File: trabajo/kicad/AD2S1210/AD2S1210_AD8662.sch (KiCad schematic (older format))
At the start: 74 parts, among them IC1 AD8662, K1 JP_1, K2 V_control, K3 Power, P1 conn_stm32f4, P2 AOUT, P3 conn_motor_control, P4 JP_2, P5 JP_3, Q1 RECOM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

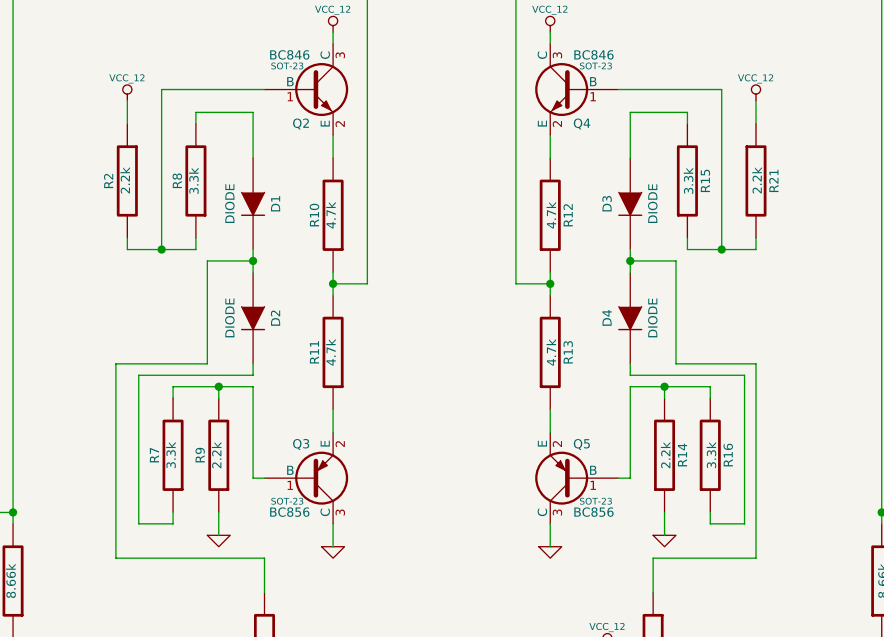
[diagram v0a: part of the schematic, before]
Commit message: correción de los valores de resistencias del buffer de tarjeta resolver
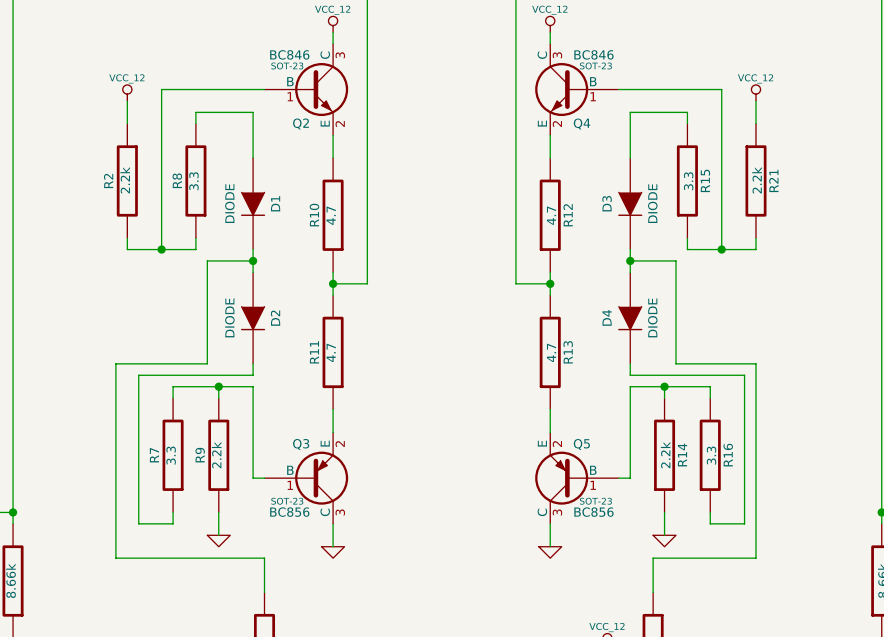
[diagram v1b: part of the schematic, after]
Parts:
- R10, R11, R12, R13: value 4.7k -> 4.7
- R15, R16, R7, R8: value 3.3k -> 3.3
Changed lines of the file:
@@
 Sheet 1 1
 Title "AD2S1210"
-Date "14 sep 2014"
+Date "13 mar 2015"
 Rev "V1.2"
 Comp "P. Koenig"
@@
 P 9900 1750
 F 0 "R15" V 9980 1750 40  0000 C CNN
-F 1 "3.3k" V 9907 1751 40  0000 C CNN
+F 1 "3.3" V 9907 1751 40  0000 C CNN
 F 2 "~" V 9830 1750 30  0000 C CNN
 F 3 "~" H 9900 1750 30  0000 C CNN
@@
 P 10000 2950
 F 0 "R16" V 10080 2950 40  0000 C CNN
-F 1 "3.3k" V 10007 2951 40  0000 C CNN
+F 1 "3.3" V 10007 2951 40  0000 C CNN
 F 2 "~" V 9930 2950 30  0000 C CNN
 F 3 "~" H 10000 2950 30  0000 C CNN
@@
 P 9300 1900
 F 0 "R12" V 9380 1900 40  0000 C CNN
-F 1 "4.7k" V 9307 1901 40  0000 C CNN
+F 1 "4.7" V 9307 1901 40  0000 C CNN
 F 2 "~" V 9230 1900 30  0000 C CNN
 F 3 "~" H 9300 1900 30  0000 C CNN
@@
 P 9300 2500
 F 0 "R13" V 9380 2500 40  0000 C CNN
-F 1 "4.7k" V 9307 2501 40  0000 C CNN
+F 1 "4.7" V 9307 2501 40  0000 C CNN
 F 2 "~" V 9230 2500 30  0000 C CNN
 F 3 "~" H 9300 2500 30  0000 C CNN
@@
 P 7750 1750
 F 0 "R8" V 7830 1750 40  0000 C CNN
-F 1 "3.3k" V 7757 1751 40  0000 C CNN
+F 1 "3.3" V 7757 1751 40  0000 C CNN
 F 2 "~" V 7680 1750 30  0000 C CNN
 F 3 "~" H 7750 1750 30  0000 C CNN
@@
 P 7650 2950
 F 0 "R7" V 7730 2950 40  0000 C CNN
-F 1 "3.3k" V 7657 2951 40  0000 C CNN
+F 1 "3.3" V 7657 2951 40  0000 C CNN
 F 2 "~" V 7580 2950 30  0000 C CNN
 F 3 "~" H 7650 2950 30  0000 C CNN
@@
 P 8350 1900
 F 0 "R10" V 8430 1900 40  0000 C CNN
-F 1 "4.7k" V 8357 1901 40  0000 C CNN
+F 1 "4.7" V 8357 1901 40  0000 C CNN
 F 2 "~" V 8280 1900 30  0000 C CNN
 F 3 "~" H 8350 1900 30  0000 C CNN
@@
 P 8350 2500
 F 0 "R11" V 8430 2500 40  0000 C CNN
-F 1 "4.7k" V 8357 2501 40  0000 C CNN
+F 1 "4.7" V 8357 2501 40  0000 C CNN
 F 2 "~" V 8280 2500 30  0000 C CNN
 F 3 "~" H 8350 2500 30  0000 C CNN
